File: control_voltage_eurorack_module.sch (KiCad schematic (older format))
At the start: 49 parts, among them J1 Conn_02x08_Odd_Even, J2 AVR-ISP-6, J3 CVOut, J4 Conn_01x04, J5 ExtClkIn, J6 TrigOut, J7 GateOut, SW1 Menu_Encoder, U1 TL072, U2 ATmega16-16AU, U3 MCP4725xxx-xCH, Y1 16M

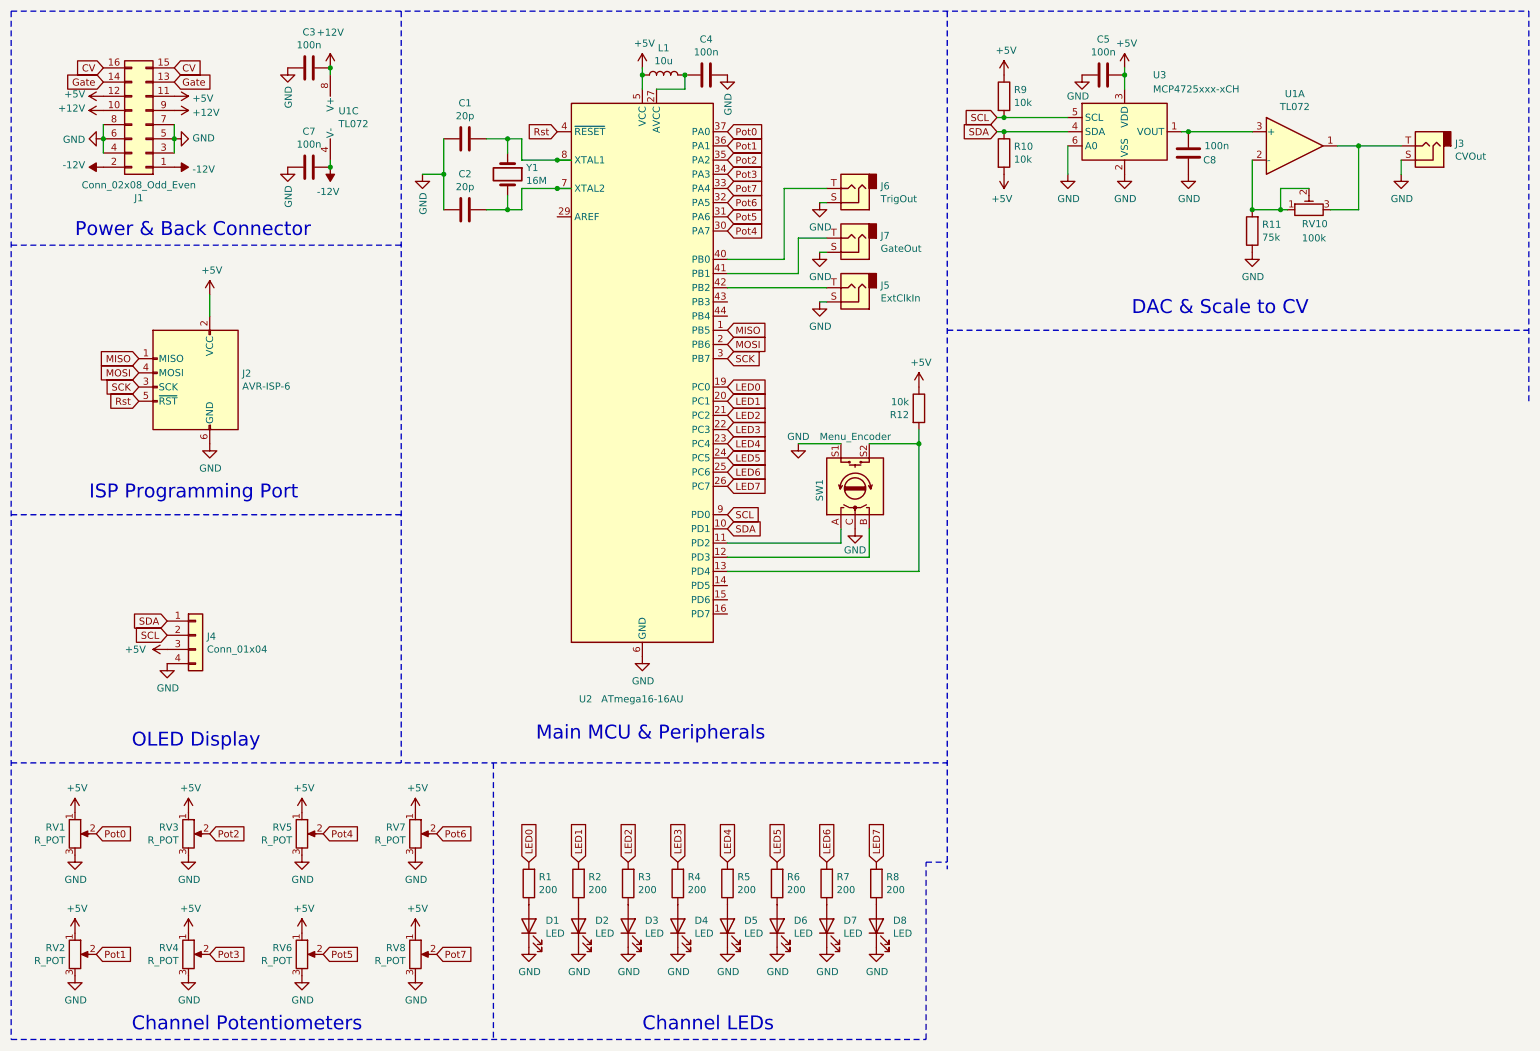
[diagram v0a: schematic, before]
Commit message: fixed wrong i2c pins and added uart port
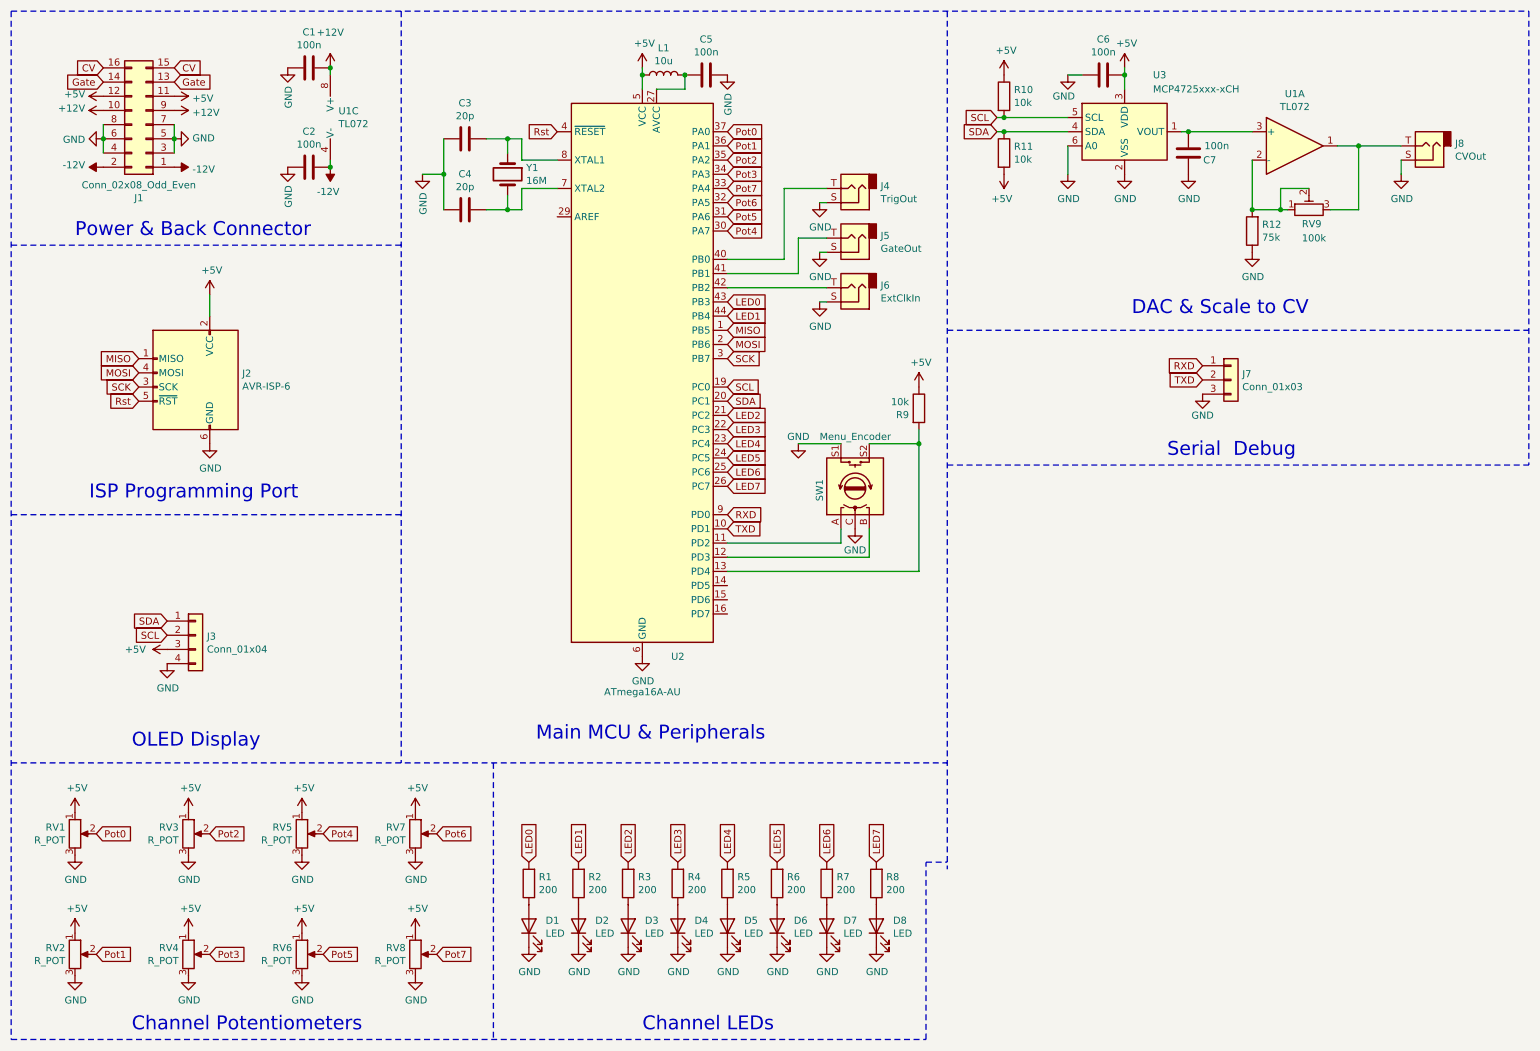
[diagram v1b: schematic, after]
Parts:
- removed U2: ATmega16-16AU, Package_QFP:TQFP-44_10x10mm_P0.8mm, symbol MCU_Microchip_ATmega:ATmega16-16AU
- added J7: Conn_01x03, Connector_PinHeader_2.54mm:PinHeader_1x03_P2.54mm_Vertical, symbol Connector_Generic:Conn_01x03
- added U2: ATmega16A-AU, Package_QFP:TQFP-44_10x10mm_P0.8mm, symbol MCU_Microchip_ATmega:ATmega16A-AU
- renumbered C3 to C1, C7 to C2, C1 to C3, C2 to C4, C4 to C5, C5 to C6, C8 to C7, J4 to J3, J6 to J4, J7 to J5, J5 to J6, J3 to J8, R9 to R10, R10 to R11, R11 to R12, R12 to R9, RV10 to RV9
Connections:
- net labels added: RXD, TXD
- wire segments 64 -> 63
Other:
- note added: "Serial Debug"
